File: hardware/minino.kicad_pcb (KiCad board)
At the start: 2 copper layers, 51 x 83.5 mm, 35 parts, among them J1 OLED, J2 GPS, J3 Battery, P1 USB_C_Plug_USB2.0, Q1 DMG3415U-7, SW1 ON, SW2 RIGHT, SW3 LEFT, SW4 DOWN, SW5 UP, SW6 OK, SW7 RESET, SW8 GPIO, U1 ESP32-S3-WROOM-1U-N16, U2 MCP73831-3-OT, U3 AP2112K-3.3

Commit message: Size_Adjustment
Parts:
- moved SW7 26.1 mm to (55.5, 76.0), turned to -90 degrees
- moved J3 20.8 mm to (52.8, 83.6), turned to 180 degrees
- moved UP 17.7 mm to (72.8, 77.5)
- moved SW2 16.4 mm to (81.4, 84.8)
- moved SW3 16.4 mm to (64.3, 84.8)
- moved Select 16.4 mm to (72.8, 84.8)
- moved SW4 15.4 mm to (72.8, 91.8)
- moved SW8 13.9 mm to (55.5, 66.8), turned to -90 degrees
- moved R8 12.2 mm to (64.3, 80.5)
- moved D4 12.2 mm to (64.3, 77.0)
- moved D3 11.9 mm to (81.3, 77.0)
- moved R7 11.9 mm to (81.3, 80.4)
- moved SW1 8.17 mm to (87.3, 83.0)
- moved R10 4.58 mm to (82.2, 57.1)
- moved P1 4.51 mm to (86.2, 52.1)
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- renumbered SW6 to Select, SW5 to UP
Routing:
- net /UP: track 62.2 -> 32.2 mm, vias 3 -> 1
- net /RST: track 29.8 -> 52.2 mm
- net /DOWN: track 69.7 -> 47.8 mm, vias 1 -> 3
- net /LED1: track 31.3 -> 9.69 mm
- net /LEFT: track 45.7 -> 25.6 mm
- net /D1: track 48.1 -> 28.7 mm, vias 0 -> 1
- net /SELECT: track 52.1 -> 39.5 mm
- net /LED2: track 26.4 -> 16.1 mm
- net /RIGHT: track 38.4 -> 28.3 mm, vias 3 -> 1
- net GND: track 12.7 -> 21.9 mm, vias 32 -> 18
- net /TX: track 18.0 -> 10.3 mm
- net /RX: track 17.4 -> 9.80 mm
- net Net-(D2-Pad1): track 31.9 -> 24.6 mm, vias 2 -> 0
- net /BOOT: track 15.3 -> 9.53 mm
- net /SCL: track 15.4 -> 10.5 mm
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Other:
- board size 51 x 83.5 mm -> 42 x 59 mm

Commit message: Add_pull_up
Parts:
- added R10: 10K, Resistor_SMD:R_0603_1608Metric, B.Cu at (60.2, 79.2)
- renumbered C4 to C2, C5 to C3, C2 to C4, C3 to C5, R7 to R6, R8 to R7, R9 to R8, R10 to R9, UP to SW5, Select to SW6
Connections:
- SW7 pad 2: /RST -> Net-(SW7-Pad2)
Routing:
- net /RST: track 52.2 -> 42.3 mm
- net Net-(SW7-Pad2): track 0.00 -> 8.30 mm
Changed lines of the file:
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@@
   (net 1 "+BATT")
   (net 2 "GND")
-  (net 3 "Net-(C2-Pad1)")
+  (net 3 "Net-(C4-Pad1)")
   (net 4 "+3V3")
   (net 5 "Net-(D1-Pad1)")
@@
   (net 52 "unconnected-(U1-Pad38)")
   (net 53 "unconnected-(U1-Pad39)")
+  (net 54 "Net-(SW7-Pad2)")
   (footprint "Button_Switch_SMD:SW_SPST_TL3342" (layer "F.Cu")
     (at 81.37 84.81 180)
@@
     (property "provedor" "LCSC")
     (attr smd)
-    (fp_text reference "R7" (at -0.32 1.41 -270) (layer "F.SilkS")
+    (fp_text reference "R6" (at -0.32 1.41 -270) (layer "F.SilkS")
       (effects (font (size 0.7 0.7) (thickness 0.15)))
     )
@@
     (property "provedor" "LCSC")
     (attr smd)
-    (fp_text reference "UP" (at 0.02 3.65) (layer "F.SilkS")
+    (fp_text reference "SW5" (at 0.02 3.65) (layer "F.SilkS")
       (effects (font (size 1 1) (thickness 0.15)))
     )
@@
     (property "provedor" "LCSC")
     (attr smd)
-    (fp_text reference "Select" (at 0 -3.75) (layer "F.SilkS")
+    (fp_text reference "SW6" (at 0 -3.75) (layer "F.SilkS")
       (effects (font (size 1 1) (thickness 0.15)))
     )
@@
     (property "provedor" "LCSC")
     (attr smd)
-    (fp_text reference "R8" (at 0.045 1.6 -270) (layer "F.SilkS")
+    (fp_text reference "R7" (at 0.045 1.6 -270) (layer "F.SilkS")
       (effects (font (size 0.7 0.7) (thickness 0.15)))
     )
@@
     (property "provedor" "LCSC")
     (attr smd)
-    (fp_text reference "R10" (at 0.13 -1.43 90) (layer "B.SilkS")
+    (fp_text reference "R9" (at 0.13 -1.43 90) (layer "B.SilkS")
       (effects (font (size 0.7 0.7) (thickness 0.15)) (justify mirror))
     )
@@
     (property "provedor" "LCSC")
     (attr smd)
-    (fp_text reference "C5" (at 2.41 0.2 90) (layer "B.SilkS")
+    (fp_text reference "C3" (at 2.41 0.2 90) (layer "B.SilkS")
       (effects (font (size 0.7 0.7) (thickness 0.15)) (justify mirror))
     )
@@
     )
   )
+  (footprint "Resistor_SMD:R_0603_1608Metric" (layer "B.Cu")
+    (at 60.23 79.25)
+    (descr "Resistor SMD 0603 (1608 Metric), square (rectangular) end terminal, IPC_7351 nominal, (Body size source: IPC-SM-782 page 72, https://www.pcb-3d.com/wordpress/wp-content/uploads/ipc-sm-782a_amendment_1_and_2.pdf), generated with kicad-footprint-generator")
+    (tags "resistor")
+    (property "LCSC#" "C15458")
+    (property "Sheetfile" "Archivo: minino.kicad_sch")
+    (property "Sheetname" "")
+    (property "manf#" "WR06X104JTL")
+    (property "provedor" "LCSC")
+    (attr smd)
+    (fp_text reference "R10" (at 0 1.43) (layer "B.SilkS")
+      (effects (font (size 1 1) (thickness 0.15)) (justify mirror))
+    )
+    (fp_text value "10K" (at 0 -1.43) (layer "B.Fab")
+      (effects (font (size 1 1) (thickness 0.15)) (justify mirror))
+    )
+    (fp_text user "${REFERENCE}" (at 0 0) (layer "B.Fab")
+      (effects (font (size 0.4 0.4) (thickness 0.06)) (justify mirror))
+    )
+    (fp_line (start -0.237258 0.5225) (end 0.237258 0.5225) (layer "B.SilkS") (width 0.12))
+    (fp_line (start -0.237258 -0.5225) (end 0.237258 -0.5225) (layer "B.SilkS") (width 0.12))
+    (fp_line (start 1.48 0.73) (end 1.48 -0.73) (layer "B.CrtYd") (width 0.05))
+    (fp_line (start -1.48 0.73) (end 1.48 0.73) (layer "B.CrtYd") (width 0.05))
+    (fp_line (start -1.48 -0.73) (end -1.48 0.73) (layer "B.CrtYd") (width 0.05))
+    (fp_line (start 1.48 -0.73) (end -1.48 -0.73) (layer "B.CrtYd") (width 0.05))
+    (fp_line (start 0.8 0.4125) (end 0.8 -0.4125) (layer "B.Fab") (width 0.1))
+    (fp_line (start 0.8 -0.4125) (end -0.8 -0.4125) (layer "B.Fab") (width 0.1))
+    (fp_line (start -0.8 0.4125) (end 0.8 0.4125) (layer "B.Fab") (width 0.1))
+    (fp_line (start -0.8 -0.4125) (end -0.8 0.4125) (layer "B.Fab") (width 0.1))
+    (pad "1" smd roundrect (at -0.825 0) (size 0.8 0.95) (layers "B.Cu" "B.Paste" "B.Mask") (roundrect_rratio 0.25)
+      (net 54 "Net-(SW7-Pad2)") (pintype "passive"))
+    (pad "2" smd roundrect (at 0.825 0) (size 0.8 0.95) (layers "B.Cu" "B.Paste" "B.Mask") (roundrect_rratio 0.25)
+      (net 26 "/RST") (pintype "passive"))
+    (model "${KICAD6_3DMODEL_DIR}/Resistor_SMD.3dshapes/R_0603_1608Metric.wrl"
+      (offset (xyz 0 0 0))
+      (scale (xyz 1 1 1))
+      (rotate (xyz 0 0 0))
+    )
+  )
   (footprint "Capacitor_SMD:C_0603_1608Metric" (layer "B.Cu")
     (at 79.12 49.96 90)
@@
     (property "provedor" "LCSC")
     (attr smd)
-    (fp_text reference "C4" (at 2.34 0.13 90) (layer "B.SilkS")
+    (fp_text reference "C2" (at 2.34 0.13 90) (layer "B.SilkS")
       (effects (font (size 0.7 0.7) (thickness 0.15)) (justify mirror))
     )
@@
     (fp_line (start 0.8 -1.45) (end -0.8 -1.45) (layer "B.Fab") (width 0.1))
     (pad "1" smd roundrect (at -1.1375 0.95 180) (size 1.325 0.6) (layers "B.Cu" "B.Paste" "B.Mask") (roundrect_rratio 0.25)
-      (net 3 "Net-(C2-Pad1)") (pinfunction "VIN") (pintype "power_in"))
+      (net 3 "Net-(C4-Pad1)") (pinfunction "VIN") (pintype "power_in"))
     (pad "2" smd roundrect (at -1.1375 0 180) (size 1.325 0.6) (layers "B.Cu" "B.Paste" "B.Mask") (roundrect_rratio 0.25)
       (net 2 "GND") (pinfunction "GND") (pintype "power_in"))
     (pad "3" smd roundrect (at -1.1375 -0.95 180) (size 1.325 0.6) (layers "B.Cu" "B.Paste" "B.Mask") (roundrect_rratio 0.25)
-      (net 3 "Net-(C2-Pad1)") (pinfunction "EN") (pintype "input"))
+      (net 3 "Net-(C4-Pad1)") (pinfunction "EN") (pintype "input"))
     (pad "4" smd roundrect (at 1.1375 -0.95 180) (size 1.325 0.6) (layers "B.Cu" "B.Paste" "B.Mask") (roundrect_rratio 0.25)
       (net 28 "unconnected-(U3-Pad4)") (pinfunction "NC") (pintype "no_connect"))
@@
     (property "provedor" "LCSC")
     (attr smd)
-    (fp_text reference "C3" (at 2.664 0) (layer "B.SilkS")
+    (fp_text reference "C5" (at 2.664 0) (layer "B.SilkS")
       (effects (font (size 0.7 0.7) (thickness 0.15)) (justify mirror))
     )
@@
       (net 2 "GND") (pinfunction "1") (pintype "passive"))
     (pad "2" smd rect (at -3.15 -1.9 270) (size 1.7 1) (layers "B.Cu" "B.Paste" "B.Mask")
-      (net 26 "/RST") (pinfunction "2") (pintype "passive"))
+      (net 54 "Net-(SW7-Pad2)") (pinfunction "2") (pintype "passive"))
     (pad "2" smd rect (at 3.15 -1.9 270) (size 1.7 1) (layers "B.Cu" "B.Paste" "B.Mask")
-      (net 26 "/RST") (pinfunction "2") (pintype "passive"))
+      (net 54 "Net-(SW7-Pad2)") (pinfunction "2") (pintype "passive"))
     (model "${KICAD6_3DMODEL_DIR}/Button_Switch_SMD.3dshapes/SW_SPST_TL3342.wrl"
       (offset (xyz 0 0 0))
@@
       (net 7 "Net-(D2-Pad1)") (pinfunction "A") (pintype "passive"))
     (pad "2" smd rect locked (at 0 1 270) (size 1.2 2.5) (layers "B.Cu" "B.Paste" "B.Mask")
-      (net 3 "Net-(C2-Pad1)") (pinfunction "B") (pintype "passive"))
+      (net 3 "Net-(C4-Pad1)") (pinfunction "B") (pintype "passive"))
     (pad "3" smd rect locked (at 2.5 1 270) (size 1.2 2.5) (layers "B.Cu" "B.Paste" "B.Mask"))
     (pad "4" thru_hole circle locked (at -3.4 -1.75 270) (size 1.4 1.4) (drill 0.9) (layers *.Cu *.Mask))
@@
     (property "provedor" "LCSC")
     (attr smd)
-    (fp_text reference "C2" (at -0.31 -1.32 90) (layer "B.SilkS")
+    (fp_text reference "C4" (at -0.31 -1.32 90) (layer "B.SilkS")
       (effects (font (size 0.7 0.7) (thickness 0.15)) (justify mirror))
     )
@@
     (fp_line (start 0.8 -0.4) (end -0.8 -0.4) (layer "B.Fab") (width 0.1))
     (pad "1" smd roundrect (at -0.775 0 270) (size 0.9 0.95) (layers "B.Cu" "B.Paste" "B.Mask") (roundrect_rratio 0.25)
-      (net 3 "Net-(C2-Pad1)") (pintype "passive"))
+      (net 3 "Net-(C4-Pad1)") (pintype "passive"))
     (pad "2" smd roundrect (at 0.775 0 270) (size 0.9 0.95) (layers "B.Cu" "B.Paste" "B.Mask") (roundrect_rratio 0.25)
       (net 2 "GND") (pintype "passive"))
@@
     (property "provedor" "LCSC")
     (attr smd)
-    (fp_text reference "R9" (at 2.41 0.25 90) (layer "B.SilkS")
+    (fp_text reference "R8" (at 2.41 0.25 90) (layer "B.SilkS")
       (effects (font (size 0.7 0.7) (thickness 0.15)) (justify mirror))
     )
@@
   (via (at 79.02 75.19) (size 0.6) (drill 0.3) (layers "F.Cu" "B.Cu") (net 26))
   (via (at 79.86 67.54) (size 0.6) (drill 0.3) (layers "F.Cu" "B.Cu") (net 26))
-  (segment (start 57.43 79.19) (end 77.55 79.19) (width 0.3) (layer "B.Cu") (net 26))
   (segment (start 80.15 56.83) (end 80.15 67.25) (width 0.3) (layer "B.Cu") (net 26))
+  (segment (start 61.055 79.25) (end 77.49 79.25) (width 0.3) (layer "B.Cu") (net 26))
+  (segment (start 79.68 56.36) (end 80.15 56.83) (width 0.3) (layer "B.Cu") (net 26))
+  (segment (start 77.49 79.25) (end 79.02 77.72) (width 0.3) (layer "B.Cu") (net 26))
+  (segment (start 77.965 56.36) (end 79.68 56.36) (width 0.3) (layer "B.Cu") (net 26))
   (segment (start 79.02 77.72) (end 79.02 75.19) (width 0.3) (layer "B.Cu") (net 26))
-  (segment (start 79.68 56.36) (end 80.15 56.83) (width 0.3) (layer "B.Cu") (net 26))
-  (segment (start 77.965 56.36) (end 79.68 56.36) (width 0.3) (layer "B.Cu") (net 26))
-  (segment (start 57.43 72.89) (end 57.43 79.19) (width 0.3) (layer "B.Cu") (net 26))
-  (segment (start 77.55 79.19) (end 79.02 77.72) (width 0.3) (layer "B.Cu") (net 26))
   (segment (start 80.15 67.25) (end 79.86 67.54) (width 0.3) (layer "B.Cu") (net 26))
   (segment (start 60.035 69.9) (end 60.465 70.33) (width 0.3) (layer "B.Cu") (net 27))
@@
   (segment (start 67.2 59.03) (end 67.2 64.44) (width 0.3) (layer "B.Cu") (net 33))
   (segment (start 71.12 68.36) (end 71.12 71.58) (width 0.3) (layer "B.Cu") (net 33))
+  (segment (start 59.405 79.25) (end 57.49 79.25) (width 0.3) (layer "B.Cu") (net 54))
+  (segment (start 57.43 72.89) (end 57.43 79.19) (width 0.3) (layer "B.Cu") (net 54))
+  (segment (start 57.49 79.25) (end 57.43 79.19) (width 0.3) (layer "B.Cu") (net 54))
   (zone (net 2) (net_name "GND") (layer "F.Cu") (hatch edge 0.508)
     (connect_pads (clearance 0.508))

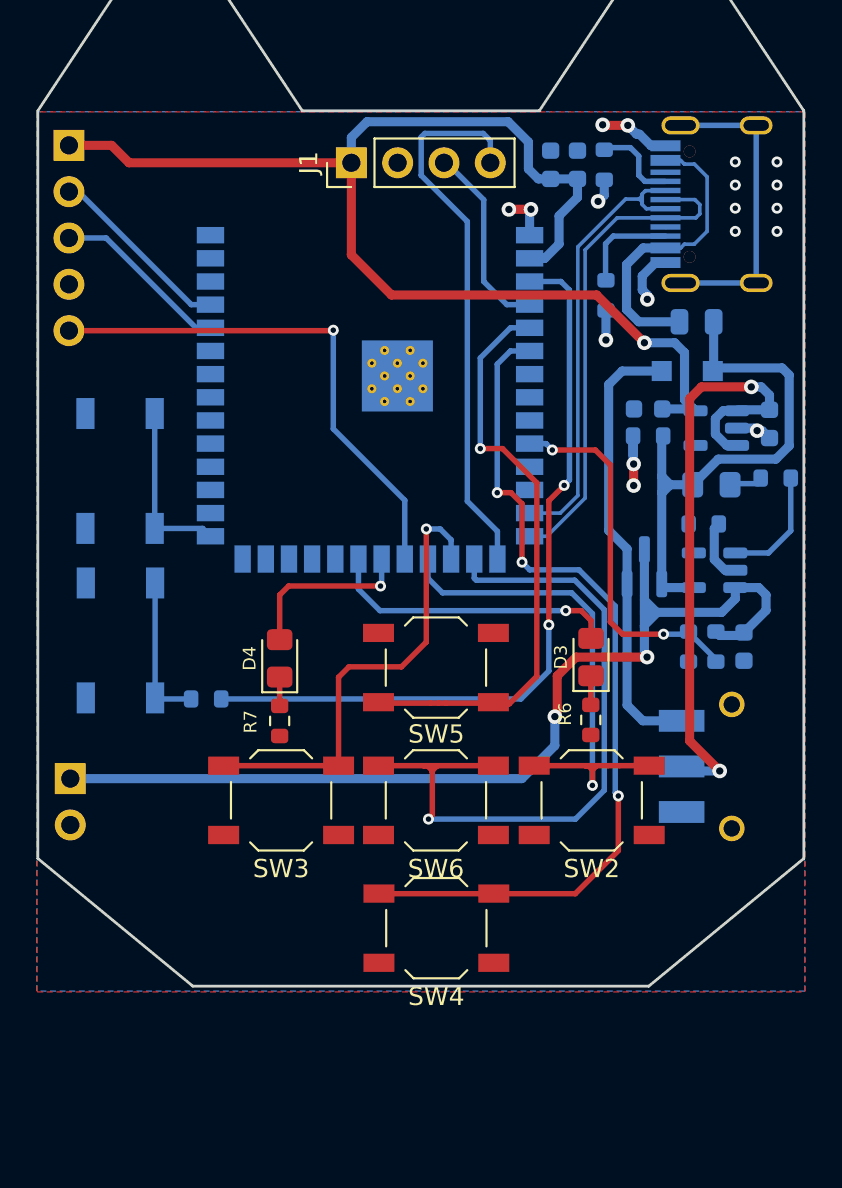
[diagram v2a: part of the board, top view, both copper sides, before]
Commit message: Add_Labels_Replace_Button
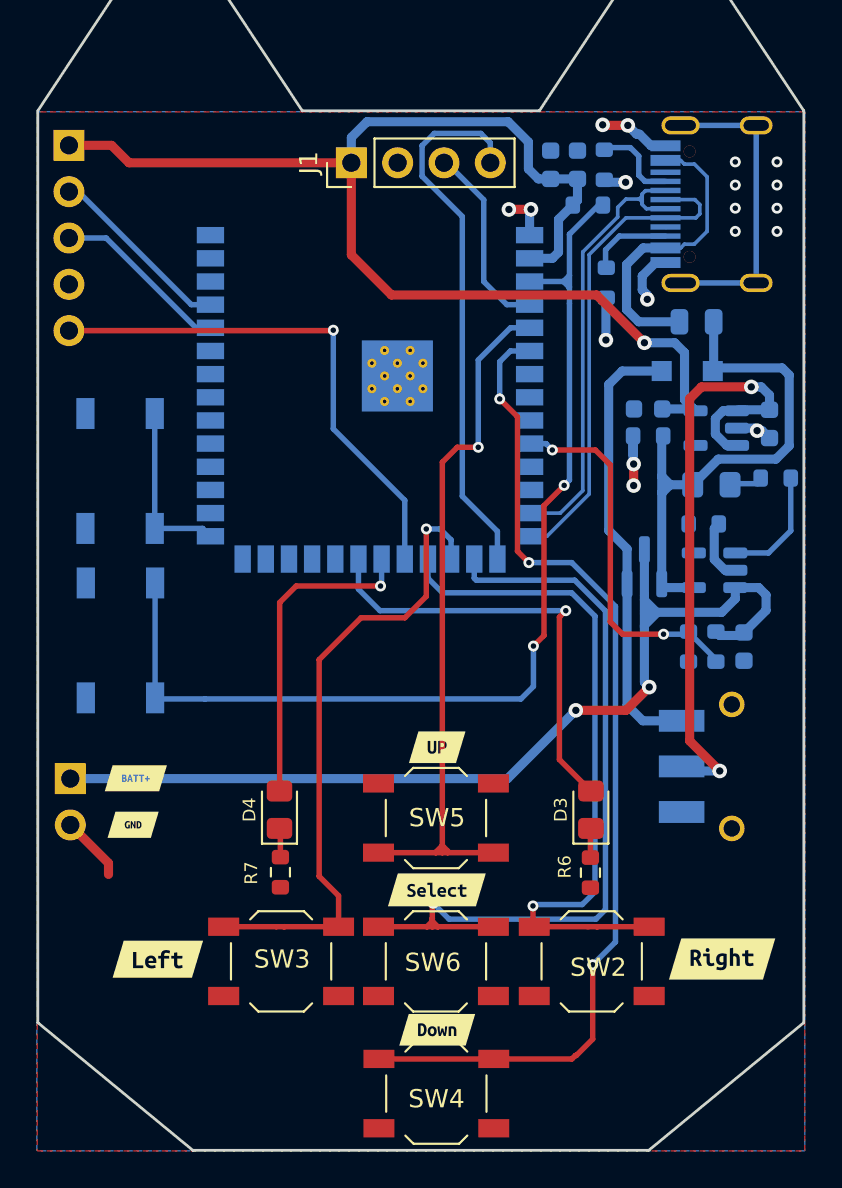
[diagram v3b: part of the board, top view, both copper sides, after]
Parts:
- added kibuzzard-6397A6E0: G***, kibuzzard-6397A6E0, F.Cu at (88.5, 93.5)
- added kibuzzard-6397A6F6: G***, kibuzzard-6397A6F6, F.Cu at (57.6, 93.5)
- added kibuzzard-6397A7B6: G***, kibuzzard-6397A7B6, F.Cu at (72.9, 81.9)
- added kibuzzard-6397A7CD: G***, kibuzzard-6397A7CD, F.Cu at (72.9, 89.7)
- added kibuzzard-6397A7DE: G***, kibuzzard-6397A7DE, F.Cu at (72.9, 97.4)
- added kibuzzard-6397B251: G***, kibuzzard-6397B251, F.Cu at (56.4, 83.6)
- added kibuzzard-6397B263: G***, kibuzzard-6397B263, F.Cu at (56.2, 86.2)
- added kibuzzard-6397B2B5: G***, kibuzzard-6397B2B5, B.Cu at (91.7, 76.7)
- added kibuzzard-6397B2CD: G***, kibuzzard-6397B2CD, B.Cu at (91.8, 89.1)
- moved R10 34.2 mm to (81.2, 52.2), turned to 180 degrees
- moved SW4 9.07 mm to (72.8, 100.9)
- moved SW2 8.83 mm to (81.4, 93.6)
- moved SW3 8.83 mm to (64.3, 93.6)
- moved SW6 8.83 mm to (72.8, 93.6)
- moved R6 8.38 mm to (81.3, 88.8)
- moved D3 8.37 mm to (81.3, 85.3)
- moved D4 8.30 mm to (64.2, 85.3)
- moved R7 8.30 mm to (64.3, 88.8)
- moved SW5 8.25 mm to (72.8, 85.8)
- moved R9 0.69 mm to (82.2, 56.4)
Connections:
- R10 pad 1: Net-(SW7-Pad2) -> /RST
- R10 pad 2: /RST -> +3V3
- SW7 pad 2: Net-(SW7-Pad2) -> /RST
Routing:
- net /RST: track 42.3 -> 58.3 mm
- net /LEFT: track 25.6 -> 35.1 mm
- net /RIGHT: track 28.3 -> 37.4 mm
- net Net-(SW7-Pad2): track 8.30 -> 0.00 mm
- net /LED2: track 16.1 -> 24.3 mm
- net /LED1: track 9.69 -> 17.7 mm
- net /DOWN: track 47.8 -> 55.7 mm
- net /UP: track 32.2 -> 39.4 mm
- net /SELECT: track 39.5 -> 44.0 mm
- net GND: track 21.9 -> 26.0 mm
- net +BATT: track 56.5 -> 55.5 mm
- net Net-(P1-PadB5): track 5.47 -> 4.60 mm
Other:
- board size 42 x 59 mm -> 42 x 68 mm

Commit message: Add_Capacitor_And__Logo
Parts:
- added C4: 10uF, Capacitor_SMD:C_0603_1608Metric, B.Cu at (81.6, 49.9)
- added G***: LOGO, Aesthetics:electronic_cats_logo_8x6, F.Cu at (62.9, 100.2)
- added G***: LOGO, Aesthetics:OSHW_MX0009, B.Cu at (72.9, 94.6)
- C2: value 22uF -> 10uF
- C3: value 100nF -> 1uF
- moved R8 0.99 mm to (83.0, 49.9), turned to -90 degrees
- moved C2 0.52 mm to (78.6, 49.9)
- moved C3 0.52 mm to (80.1, 49.9)
- moved R10 0.31 mm to (80.9, 52.1)
- renumbered C4 to C5, C5 to C6
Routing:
- net Net-(P1-PadA5): track 4.78 -> 2.46 mm
- net GND: track 26.0 -> 24.8 mm, vias 18 -> 17
- net +3V3: track 69.2 -> 70.3 mm
- net /UP: track 39.4 -> 40.0 mm

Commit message: Add_BOM_And_Labels
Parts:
- removed the G*** at (72.9, 94.6)
- added kibuzzard-6398BE5A: G***, kibuzzard-6398BE5A, B.Cu at (51.8, 66.8)
- added kibuzzard-6398BE6D: G***, kibuzzard-6398BE6D, B.Cu at (51.7, 76.2)
- G***, kibuzzard-6397B251, kibuzzard-6397B263: moved to B.Cu
- kibuzzard-6397B2B5, kibuzzard-6397B2CD: moved to F.Cu
- moved G*** 9.89 mm to (72.0, 96.2), turned to 180 degrees
- turned kibuzzard-6397B251 to 180 degrees
- turned kibuzzard-6397B263 to 180 degrees
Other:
- board text added: "Minino V1.0"

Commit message: Add_Logo
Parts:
- added REF**: OSHW-Symbol_6.7x6mm_Copper, Symbol:OSHW-Symbol_6.7x6mm_Copper, F.Cu at (80.2, 95.7)
- added kibuzzard-6398F328: G***, kibuzzard-6398F328, B.Cu at (84.7, 67.4)
- moved G*** 7.77 mm to (64.2, 96.2)
